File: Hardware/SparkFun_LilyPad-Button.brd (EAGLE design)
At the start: 15.7 x 8 mm, 6 parts

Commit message: Clean up a few things
Ready for review
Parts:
- moved JP12 1.14 mm to (11.7, 4.01)
- moved JP13 1.14 mm to (4.06, 4.01)
- moved S4 1.14 mm to (7.87, 4.01)
- moved U$45 1.14 mm to (7.87, 4.01)
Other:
- board text added: "Inches"
- board text added: "Unplated holes: 0.013"
- board text removed: "Unplated holes: 0.02"

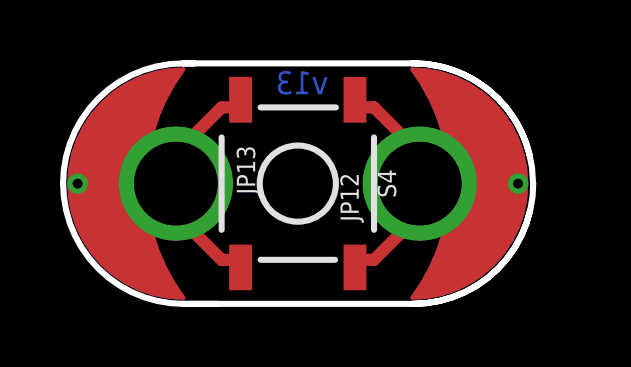
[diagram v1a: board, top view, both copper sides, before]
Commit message: Changed to v20
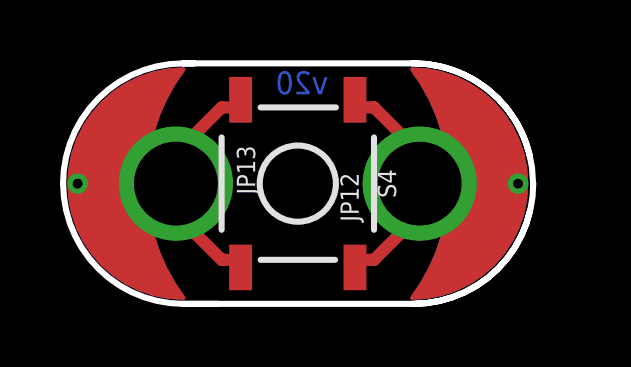
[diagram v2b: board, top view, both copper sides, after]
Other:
- board text added: "v20"
- board text removed: "v13"
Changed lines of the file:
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@@
 <layer number="38" name="bTest" color="7" fill="1" visible="no" active="no"/>
 <layer number="43" name="vRestrict" color="2" fill="10" visible="no" active="no"/>
-<layer number="47" name="Measures" color="7" fill="1" visible="yes" active="yes"/>
+<layer number="47" name="Measures" color="7" fill="1" visible="no" active="yes"/>
 <layer number="48" name="Document" color="7" fill="1" visible="no" active="no"/>
 <layer number="49" name="Reference" color="13" fill="1" visible="no" active="yes"/>
@@
 <text x="-8.943340625" y="-15.4178" size="1.778" layer="51" font="vector">Revised by: Elias Santistevan</text>
 <text x="-19.05" y="-18.57375" size="1.778" layer="51" font="vector" align="top-left">LilyPad concept and shapes by:  L. Buechley and N. Seidle</text>
-<text x="8.89" y="6.9875375" size="0.762" layer="16" font="vector" ratio="15" rot="MR0">v13</text>
+<text x="8.89" y="6.9875375" size="0.762" layer="16" font="vector" ratio="15" rot="MR0">v20</text>
 <dimension x1="0.048259375" y1="4.00811875" x2="15.71498125" y2="4.02081875" x3="7.874584375" y3="12.694028125" textsize="1.778" textratio="15" layer="47" unit="inch"/>
 <dimension x1="4.064" y1="8.01655625" x2="4.064" y2="0" x3="21.59" y3="4.008278125" textsize="1.778" textratio="15" layer="47" unit="inch"/>

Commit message: Super fine adjustment of text
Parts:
- turned U$45 to 0 degrees
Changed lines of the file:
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@@
 <layer number="47" name="Measures" color="7" fill="1" visible="no" active="yes"/>
 <layer number="48" name="Document" color="7" fill="1" visible="no" active="no"/>
-<layer number="49" name="Reference" color="13" fill="1" visible="no" active="yes"/>
+<layer number="49" name="Reference" color="13" fill="1" visible="yes" active="yes"/>
 <layer number="50" name="dxf" color="7" fill="1" visible="no" active="no"/>
 <layer number="52" name="bDocu" color="7" fill="1" visible="no" active="no"/>
@@
 <text x="16.51" y="-39.37" size="1.778" layer="52" rot="MR0" align="top-left">Solder mask color: Purple (Lilypad)</text>
 <text x="16.51" y="-43.18" size="1.778" layer="52" rot="MR0" align="top-left">Finishing: Lead-free HASL</text>
-<text x="4.8180625" y="1.90468125" size="1.27" layer="22" font="vector" ratio="15" rot="MR180">Button</text>
+<text x="4.6910625" y="1.90468125" size="1.27" layer="22" font="vector" ratio="15" rot="MR180">Button</text>
 <wire x1="4.953" y1="4.00811875" x2="1.651" y2="4.00811875" width="0.4064" layer="29"/>
 <wire x1="13.081" y1="4.00811875" x2="16.16075" y2="4.00811875" width="0.4064" layer="29"/>
@@
 <wire x1="15.7226" y1="4.0132" x2="11.7094" y2="0" width="0.2032" layer="20" curve="-90"/>
 <wire x1="15.71498125" y1="4.02081875" x2="11.719559375" y2="8.023859375" width="0.2032" layer="20" curve="90"/>
+<text x="17.78" y="-34.29" size="1.778" layer="52" rot="MR0" align="top-left">PCB thickness: 31 mil / 0.8mm </text>
+<text x="17.78" y="-38.1" size="1.778" layer="52" rot="MR0" align="top-left">Solder mask color: Purple (Lilypad)</text>
+<text x="17.78" y="-41.91" size="1.778" layer="52" rot="MR0" align="top-left">Finishing: Lead-free HASL</text>
+<text x="17.78" y="-45.72" size="1.778" layer="52" rot="MR0" align="top-left">Unplated holes:
+0.013
+</text>
+<text x="-8.89" y="-45.72" size="1.778" layer="52" rot="MR0" align="top-left">Plated holes:
+0.11
+</text>
+<text x="-9.97711875" y="-12.8016" size="1.778" layer="52" font="vector" rot="MR0">Marshal Taylor</text>
+<text x="8.943340625" y="-15.4178" size="1.778" layer="52" font="vector" rot="MR0">Revised by: Elias Santistevan</text>
+<text x="19.05" y="-18.57375" size="1.778" layer="52" font="vector" rot="MR0" align="top-left">LilyPad concept and shapes by:  L. Buechley and N. Seidle</text>
+<text x="8.89" y="6.9875375" size="0.762" layer="16" font="vector" ratio="15" rot="MR0">v20</text>
+<dimension x1="0.048259375" y1="4.00811875" x2="15.71498125" y2="4.02081875" x3="7.874584375" y3="12.694028125" textsize="1.778" textratio="15" layer="47" unit="inch"/>
+<dimension x1="4.064" y1="8.01655625" x2="4.064" y2="0" x3="21.59" y3="4.008278125" textsize="1.778" textratio="15" layer="47" unit="inch"/>
+<text x="3.683" y="10.16" size="1.778" layer="47" font="vector" ratio="15">Inches</text>
+<text x="-130.81" y="-36.83" size="1.778" layer="52" rot="MR0" align="top-left">PCB thickness: 31 mil / 0.8mm </text>
+<text x="-130.81" y="-40.64" size="1.778" layer="52" rot="MR0" align="top-left">Solder mask color: Purple (Lilypad)</text>
+<text x="-130.81" y="-44.45" size="1.778" layer="52" rot="MR0" align="top-left">Finishing: Lead-free HASL</text>
+<text x="-130.81" y="-48.26" size="1.778" layer="52" rot="MR0" align="top-left">Unplated holes:
+0.013
+</text>
+<text x="-157.48" y="-48.26" size="1.778" layer="52" rot="MR0" align="top-left">Plated holes:
+0.11
+</text>
+<text x="-158.56711875" y="-15.3416" size="1.778" layer="52" font="vector" rot="MR0">Marshal Taylor</text>
+<text x="-139.646659375" y="-17.9578" size="1.778" layer="52" font="vector" rot="MR0">Revised by: Elias Santistevan</text>
+<text x="-129.54" y="-21.11375" size="1.778" layer="52" font="vector" rot="MR0" align="top-left">LilyPad concept and shapes by:  L. Buechley and N. Seidle</text>
 <text x="-17.78" y="-34.29" size="1.778" layer="51" align="top-left">PCB thickness: 31 mil / 0.8mm </text>
 <text x="-17.78" y="-38.1" size="1.778" layer="51" align="top-left">Solder mask color: Purple (Lilypad)</text>
@@
 <text x="-8.943340625" y="-15.4178" size="1.778" layer="51" font="vector">Revised by: Elias Santistevan</text>
 <text x="-19.05" y="-18.57375" size="1.778" layer="51" font="vector" align="top-left">LilyPad concept and shapes by:  L. Buechley and N. Seidle</text>
-<text x="8.89" y="6.9875375" size="0.762" layer="16" font="vector" ratio="15" rot="MR0">v20</text>
-<dimension x1="0.048259375" y1="4.00811875" x2="15.71498125" y2="4.02081875" x3="7.874584375" y3="12.694028125" textsize="1.778" textratio="15" layer="47" unit="inch"/>
-<dimension x1="4.064" y1="8.01655625" x2="4.064" y2="0" x3="21.59" y3="4.008278125" textsize="1.778" textratio="15" layer="47" unit="inch"/>
-<text x="3.683" y="10.16" size="1.778" layer="47" font="vector" ratio="15">Inches</text>
 </plain>
 <attributes>
@@
 <element name="JP13" library="LilyPad-Wearables" package="PETAL-MEDIUM-2SIDE" value="SEWTAP_MEDIUM-2SIDE" x="4.064" y="4.00811875" rot="R270"/>
 <element name="JP12" library="LilyPad-Wearables" package="PETAL-MEDIUM-2SIDE" value="SEWTAP_MEDIUM-2SIDE" x="11.684" y="4.00811875" rot="R90"/>
-<element name="U$45" library="LilyPad-Wearables" package="LOGO-L" value="" x="7.874" y="4.00811875" rot="MR180"/>
+<element name="U$45" library="LilyPad-Wearables" package="LOGO-L" value="" x="7.874" y="3.99288125" rot="MR0"/>
 <element name="S4" library="SparkFun-Switches" package="TACTILE_SWITCH_SMD_5.2MM" value="MOMENTARY-SWITCH-SPST-SMD-5.2-REDUNDANT" x="7.874" y="4.00811875" rot="R270">
 <attribute name="PROD_ID" value="SWCH-08247" x="7.874" y="4.00811875" size="1.778" layer="27" rot="R270" display="off"/>
